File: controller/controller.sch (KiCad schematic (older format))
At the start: 46 parts, among them J1 Conn_01x25_Membrane, J2 Conn_01x04, SW1 SW_Push, SW2 SW_Push, U1 AMS1117-3.3, U2 STM32F303RCT6, U3 TPS2553DBVR, U4 USBLC6-2SC6, Y1 16MHz

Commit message: added solenoid driver
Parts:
- added J3: Conn_Solenoid_Driver, Connector_JST:JST_PH_S4B-PH-K_1x04_P2.00mm_Horizontal, symbol Connector_Generic:Conn_01x04
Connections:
- net labels added: SOLENOID_ENABLE, SOLENOID_TRIGGER
- wire segments 115 -> 117
- no-connect marks 19 -> 17
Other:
- note added: "GPIO PC13..PC15 output mode\ncurrent is limited"
- note removed: "Do not use GPIO PC13..PC15 in output mode\n(current is limited)"
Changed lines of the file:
@@
 	7925 5025 7450 5025
-$Comp
-L MCU_ST_STM32F3:STM32F303RCTx U2
-U 1 1 5FCE2F71
-P 4450 4325
-F 0 "U2" H 3875 2550 50  0000 C CNN
-F 1 "STM32F303RCT6" H 5025 2550 50  0000 C CNN
-F 2 "Package_QFP:LQFP-64_10x10mm_P0.5mm" H 3850 2625 50  0001 R CNN
-F 3 "https://datasheet.lcsc.com/szlcsc/1811182038_STMicroelectronics-STM32F303RCT6_C65361.pdf" H 4450 4325 50  0001 C CNN
-F 4 "C65361" H 4450 4325 50  0001 C CNN "LCSC"
-	1    4450 4325
-	1    0    0    -1
-$EndComp
 $Comp
 L Regulator_Linear:AMS1117-3.3 U1
@@
 NoConn ~ 5150 4225
 NoConn ~ 5150 4025
-Text Notes 5225 4175 0    50   ~ 0
-Do not use GPIO PC13..PC15 in output mode\n(current is limited)
+Text Notes 2625 6150 0    50   ~ 0
+GPIO PC13..PC15 output mode\ncurrent is limited
 Text GLabel 5350 3825 2    50   BiDi ~ 0
 USB_DM
@@
 NoConn ~ 3750 4225
 NoConn ~ 3750 4025
-NoConn ~ 3750 5725
 NoConn ~ 3750 5825
 NoConn ~ 3750 5925
@@
 NoConn ~ 5150 4725
 NoConn ~ 5150 4825
-NoConn ~ 5150 4925
 NoConn ~ 5150 5025
 NoConn ~ 5150 5125
@@
 	1    0    0    -1
 $EndComp
+$Comp
+L Connector_Generic:Conn_01x04 J3
+U 1 1 600024AB
+P 6100 7025
+F 0 "J3" H 6180 7017 50  0000 L CNN
+F 1 "Conn_Solenoid_Driver" H 6180 6926 50  0000 L CNN
+F 2 "Connector_JST:JST_PH_S4B-PH-K_1x04_P2.00mm_Horizontal" H 6100 7025 50  0001 C CNN
+F 3 "~" H 6100 7025 50  0001 C CNN
+F 4 "https://www.tme.eu/ro/katalog/conectori-de-semnal_30/?s_field=1000011&s_order=desc&search=jst&visible_params=412%2C2%2C6%2C613%2C422%2C7%2C426%2C9%2C416%2C77%2C18%2C32%2C1247%2C2555%2C418%2C419%2C1322%2C516%2C5%2C82%2C743%2C424%2C425%2C11%2C45&mapped_params=412%3A1443412%3B426%3A1443403%3B" H 6100 7025 50  0001 C CNN "Notes"
+	1    6100 7025
+	1    0    0    -1
+$EndComp
+$Comp
+L power:VBUS #PWR0108
+U 1 1 6000A0FD
+P 5825 6900
+F 0 "#PWR0108" H 5825 6750 50  0001 C CNN
+F 1 "VBUS" H 5950 7025 50  0000 C CNN
+F 2 "" H 5825 6900 50  0001 C CNN
+F 3 "" H 5825 6900 50  0001 C CNN
+	1    5825 6900
+	1    0    0    -1
+$EndComp
+Wire Wire Line
+	5825 6900 5825 6925
+Wire Wire Line
+	5825 6925 5900 6925
+$Comp
+L power:GND #PWR0109
+U 1 1 6000F2BB
+P 5900 7225
+F 0 "#PWR0109" H 5900 6975 50  0001 C CNN
+F 1 "GND" V 5905 7097 50  0000 R CNN
+F 2 "" H 5900 7225 50  0001 C CNN
+F 3 "" H 5900 7225 50  0001 C CNN
+	1    5900 7225
+	0    1    1    0
+$EndComp
+Text GLabel 5900 7125 0    50   BiDi ~ 0
+SOLENOID_ENABLE
+Text GLabel 5900 7025 0    50   BiDi ~ 0
+SOLENOID_TRIGGER
+Text GLabel 3750 5725 0    50   BiDi ~ 0
+SOLENOID_ENABLE
+Text GLabel 5150 4925 2    50   BiDi ~ 0
+SOLENOID_TRIGGER
+$Comp
+L MCU_ST_STM32F3:STM32F303RCTx U2
+U 1 1 5FCE2F71
+P 4450 4325
+F 0 "U2" H 3875 2550 50  0000 C CNN
+F 1 "STM32F303RCT6" H 5025 2550 50  0000 C CNN
+F 2 "Package_QFP:LQFP-64_10x10mm_P0.5mm" H 3850 2625 50  0001 R CNN
+F 3 "https://datasheet.lcsc.com/szlcsc/1811182038_STMicroelectronics-STM32F303RCT6_C65361.pdf" H 4450 4325 50  0001 C CNN
+F 4 "C65361" H 4450 4325 50  0001 C CNN "LCSC"
+	1    4450 4325
+	1    0    0    -1
+$EndComp

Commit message: added gpio header and other updates
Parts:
- added J4: Conn_01x04, Connector_PinHeader_2.54mm:PinHeader_1x04_P2.54mm_Vertical, symbol Connector_Generic:Conn_01x04
- added J5: Conn_01x07, Connector_PinHeader_2.54mm:PinHeader_1x07_P2.54mm_Vertical, symbol Connector_Generic:Conn_01x07
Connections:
- net labels added: GPIO_PA0, GPIO_PA1, GPIO_PA2, GPIO_PC3, UART_RX, UART_TX
- wire segments 117 -> 130
- no-connect marks 17 -> 12
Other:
- note added: "PA10 (UART RX) pulled high to make sure it's not\nmisinterpreted during bootloader mode."
- note added: "PA9 (UART TX) could be output during bootloader mode"
- note removed: "PA10 pulled high to make sure it's not\nmisinterpreted during bootloader mode."
- note removed: "PA9 could be output during bootloader mode"
- moved on the sheet: R8
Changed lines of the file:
@@
 Text GLabel 5150 3025 2    50   BiDi ~ 0
 MEMBRANE21
-Text GLabel 3750 4725 0    50   BiDi ~ 0
+Text GLabel 3550 4200 0    50   BiDi ~ 0
 MEMBRANE22
-Text GLabel 5150 2925 2    50   BiDi ~ 0
+Text GLabel 3750 4425 0    50   BiDi ~ 0
 MEMBRANE23
-Text GLabel 5150 2825 2    50   BiDi ~ 0
+Text GLabel 3750 4525 0    50   BiDi ~ 0
 MEMBRANE24
-Text GLabel 5150 2725 2    50   BiDi ~ 0
+Text GLabel 3750 4625 0    50   BiDi ~ 0
 MEMBRANE25
-NoConn ~ 5150 3625
-Text Notes 5225 3650 0    50   ~ 0
-PA9 could be output during bootloader mode
+Text Notes 5975 3650 0    50   ~ 0
+PA9 (UART TX) could be output during bootloader mode
 $Comp
 L Device:R R8
 U 1 1 6012C331
-P 5300 3725
-F 0 "R8" V 5250 3875 50  0000 C CNN
-F 1 "62k" V 5300 3725 50  0000 C CNN
-F 2 "Resistor_SMD:R_0805_2012Metric_Pad1.15x1.40mm_HandSolder" V 5230 3725 50  0001 C CNN
-F 3 "~" H 5300 3725 50  0001 C CNN
-F 4 "C17783" H 5300 3725 50  0001 C CNN "LCSC"
-	1    5300 3725
+P 6500 4000
+F 0 "R8" V 6450 4150 50  0000 C CNN
+F 1 "62k" V 6500 4000 50  0000 C CNN
+F 2 "Resistor_SMD:R_0805_2012Metric_Pad1.15x1.40mm_HandSolder" V 6430 4000 50  0001 C CNN
+F 3 "~" H 6500 4000 50  0001 C CNN
+F 4 "C17783" H 6500 4000 50  0001 C CNN "LCSC"
+	1    6500 4000
 	0    1    1    0
 $EndComp
@@
 L power:+3.3V #PWR0105
 U 1 1 60130C5B
-P 5450 3725
-F 0 "#PWR0105" H 5450 3575 50  0001 C CNN
-F 1 "+3.3V" V 5465 3853 50  0000 L CNN
-F 2 "" H 5450 3725 50  0001 C CNN
-F 3 "" H 5450 3725 50  0001 C CNN
-	1    5450 3725
+P 6650 4000
+F 0 "#PWR0105" H 6650 3850 50  0001 C CNN
+F 1 "+3.3V" V 6665 4128 50  0000 L CNN
+F 2 "" H 6650 4000 50  0001 C CNN
+F 3 "" H 6650 4000 50  0001 C CNN
+	1    6650 4000
 	0    1    1    0
 $EndComp
-Text Notes 5850 3825 0    50   ~ 0
-PA10 pulled high to make sure it's not\nmisinterpreted during bootloader mode.
+Text Notes 6075 3825 0    50   ~ 0
+PA10 (UART RX) pulled high to make sure it's not\nmisinterpreted during bootloader mode.
 Text GLabel 6750 5025 0    50   BiDi ~ 0
 LEDDRV1
@@
 LEDDRV3
 NoConn ~ 3750 4225
-NoConn ~ 3750 4025
 NoConn ~ 3750 5825
 NoConn ~ 3750 5925
@@
 Wire Wire Line
 	7975 6100 8025 6100
-NoConn ~ 3750 4425
-NoConn ~ 3750 4525
-NoConn ~ 3750 4625
 NoConn ~ 5150 4725
 NoConn ~ 5150 4825
@@
 	1    0    0    -1
 $EndComp
+Wire Wire Line
+	3550 4200 3600 4200
+Wire Wire Line
+	3600 4200 3600 4025
+Wire Wire Line
+	3600 4025 3750 4025
+$Comp
+L Connector_Generic:Conn_01x04 J4
+U 1 1 5FDF4DBB
+P 7200 4550
+F 0 "J4" H 7118 4125 50  0000 C CNN
+F 1 "Conn_01x04" H 7118 4216 50  0000 C CNN
+F 2 "Connector_PinHeader_2.54mm:PinHeader_1x04_P2.54mm_Vertical" H 7200 4550 50  0001 C CNN
+F 3 "~" H 7200 4550 50  0001 C CNN
+	1    7200 4550
+	-1   0    0    1
+$EndComp
+Text GLabel 5150 3625 2    50   BiDi ~ 0
+UART_TX
+Text GLabel 7400 4550 2    50   BiDi ~ 0
+UART_TX
+Text GLabel 5150 3725 2    50   BiDi ~ 0
+UART_RX
+Text GLabel 6350 4000 0    50   BiDi ~ 0
+UART_RX
+Text GLabel 7400 4450 2    50   BiDi ~ 0
+UART_RX
+$Comp
+L power:GND #PWR030
+U 1 1 5FE1A17C
+P 7675 4700
+F 0 "#PWR030" H 7675 4450 50  0001 C CNN
+F 1 "GND" H 7675 4550 50  0000 C CNN
+F 2 "" H 7675 4700 50  0001 C CNN
+F 3 "" H 7675 4700 50  0001 C CNN
+	1    7675 4700
+	1    0    0    -1
+$EndComp
+$Comp
+L power:+3.3V #PWR029
+U 1 1 5FE1A75A
+P 7675 4325
+F 0 "#PWR029" H 7675 4175 50  0001 C CNN
+F 1 "+3.3V" H 7690 4498 50  0000 C CNN
+F 2 "" H 7675 4325 50  0001 C CNN
+F 3 "" H 7675 4325 50  0001 C CNN
+	1    7675 4325
+	1    0    0    -1
+$EndComp
+Wire Wire Line
+	7675 4350 7675 4325
+Text GLabel 5150 2725 2    50   BiDi ~ 0
+GPIO_PA0
+Text GLabel 5150 2825 2    50   BiDi ~ 0
+GPIO_PA1
+Text GLabel 5150 2925 2    50   BiDi ~ 0
+GPIO_PA2
+Text GLabel 3750 4725 0    50   BiDi ~ 0
+GPIO_PC3
+Text GLabel 10275 5450 0    50   BiDi ~ 0
+GPIO_PA0
+Text GLabel 10275 5550 0    50   BiDi ~ 0
+GPIO_PA1
+Text GLabel 10275 5750 0    50   BiDi ~ 0
+GPIO_PA2
+Text GLabel 10275 5850 0    50   BiDi ~ 0
+GPIO_PC3
+$Comp
+L power:GND #PWR032
+U 1 1 5FE70830
+P 9750 5725
+F 0 "#PWR032" H 9750 5475 50  0001 C CNN
+F 1 "GND" H 9750 5575 50  0000 C CNN
+F 2 "" H 9750 5725 50  0001 C CNN
+F 3 "" H 9750 5725 50  0001 C CNN
+	1    9750 5725
+	1    0    0    -1
+$EndComp
+$Comp
+L power:+3.3V #PWR031
+U 1 1 5FE7203C
+P 9500 5850
+F 0 "#PWR031" H 9500 5700 50  0001 C CNN
+F 1 "+3.3V" H 9515 6023 50  0000 C CNN
+F 2 "" H 9500 5850 50  0001 C CNN
+F 3 "" H 9500 5850 50  0001 C CNN
+	1    9500 5850
+	1    0    0    -1
+$EndComp
+$Comp
+L Connector_Generic:Conn_01x07 J5
+U 1 1 5FEB4462
+P 10475 5650
+F 0 "J5" H 10555 5692 50  0000 L CNN
+F 1 "Conn_01x07" H 10555 5601 50  0000 L CNN
+F 2 "Connector_PinHeader_2.54mm:PinHeader_1x07_P2.54mm_Vertical" H 10475 5650 50  0001 C CNN
+F 3 "~" H 10475 5650 50  0001 C CNN
+	1    10475 5650
+	1    0    0    -1
+$EndComp
+$Comp
+L power:VBUS #PWR033
+U 1 1 5FEC2379
+P 10175 5275
+F 0 "#PWR033" H 10175 5125 50  0001 C CNN
+F 1 "VBUS" H 10190 5448 50  0000 C CNN
+F 2 "" H 10175 5275 50  0001 C CNN
+F 3 "" H 10175 5275 50  0001 C CNN
+	1    10175 5275
+	1    0    0    -1
+$EndComp
+Wire Wire Line
+	10175 5275 10175 5350
+Wire Wire Line
+	10175 5350 10275 5350
+Wire Wire Line
+	9750 5725 9750 5650
+Wire Wire Line
+	9750 5650 10275 5650
+Wire Wire Line
+	9500 5950 9500 5850
+Wire Wire Line
+	9500 5950 10275 5950
+Wire Wire Line
+	7400 4350 7675 4350
+Wire Wire Line
+	7400 4650 7675 4650
+Wire Wire Line
+	7675 4650 7675 4700
 $EndSCHEMATC

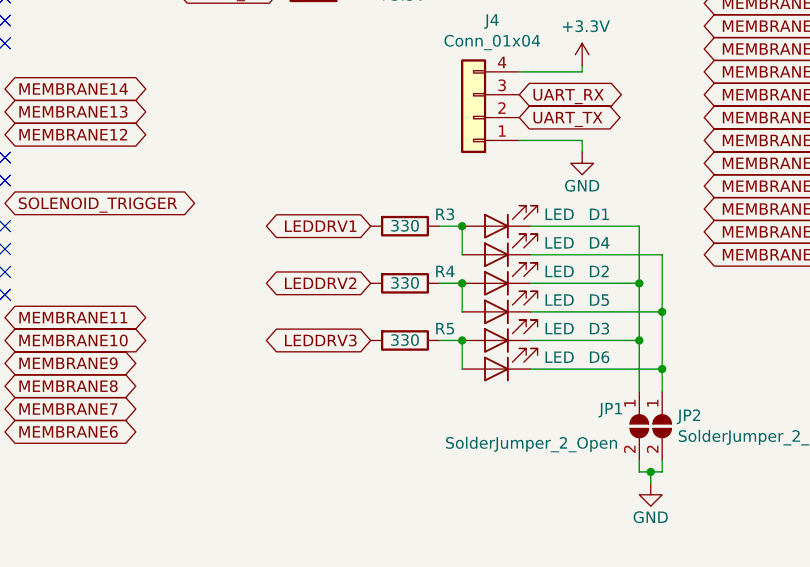
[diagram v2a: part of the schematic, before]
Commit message: LED current limit resistors changed to 47 ohm
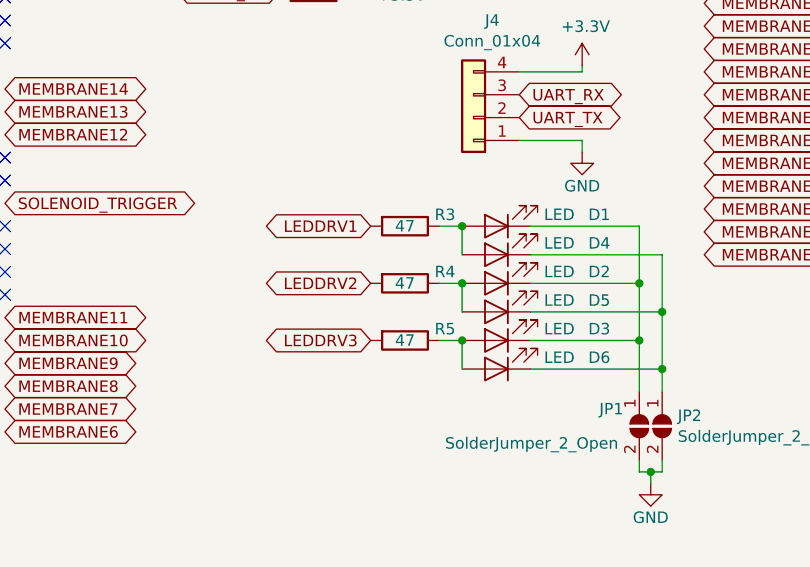
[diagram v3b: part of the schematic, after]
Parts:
- R3, R4, R5: value 330 -> 47; LCSC C17630 -> C17714
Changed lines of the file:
@@
 P 6900 5025
 F 0 "R3" V 6850 5200 50  0000 C CNN
-F 1 "330" V 6900 5025 50  0000 C CNN
+F 1 "47" V 6900 5025 50  0000 C CNN
 F 2 "Resistor_SMD:R_0805_2012Metric_Pad1.15x1.40mm_HandSolder" V 6830 5025 50  0001 C CNN
 F 3 "~" H 6900 5025 50  0001 C CNN
-F 4 "C17630" H 6900 5025 50  0001 C CNN "LCSC"
+F 4 "C17714" H 6900 5025 50  0001 C CNN "LCSC"
 	1    6900 5025
 	0    1    1    0
@@
 P 6900 5275
 F 0 "R4" V 6850 5450 50  0000 C CNN
-F 1 "330" V 6900 5275 50  0000 C CNN
+F 1 "47" V 6900 5275 50  0000 C CNN
 F 2 "Resistor_SMD:R_0805_2012Metric_Pad1.15x1.40mm_HandSolder" V 6830 5275 50  0001 C CNN
 F 3 "~" H 6900 5275 50  0001 C CNN
-F 4 "C17630" H 6900 5275 50  0001 C CNN "LCSC"
+F 4 "C17714" H 6900 5275 50  0001 C CNN "LCSC"
 	1    6900 5275
 	0    1    1    0
@@
 P 6900 5525
 F 0 "R5" V 6850 5700 50  0000 C CNN
-F 1 "330" V 6900 5525 50  0000 C CNN
+F 1 "47" V 6900 5525 50  0000 C CNN
 F 2 "Resistor_SMD:R_0805_2012Metric_Pad1.15x1.40mm_HandSolder" V 6830 5525 50  0001 C CNN
 F 3 "~" H 6900 5525 50  0001 C CNN
-F 4 "C17630" H 6900 5525 50  0001 C CNN "LCSC"
+F 4 "C17714" H 6900 5525 50  0001 C CNN "LCSC"
 	1    6900 5525
 	0    1    1    0
@@
 F 1 "LED" H 7025 4975 50  0000 C CNN
 F 2 "LED_SMD:LED_0805_2012Metric_Pad1.15x1.40mm_HandSolder" H 7300 5025 50  0001 C CNN
-F 3 "~" H 7300 5025 50  0001 C CNN
+F 3 "https://datasheet.lcsc.com/szlcsc/Hubei-KENTO-Elec-17-21SUYC-TR8_C2296.pdf" H 7300 5025 50  0001 C CNN
 F 4 "C2296" H 7300 5025 50  0001 C CNN "LCSC"
 	1    7300 5025
@@
 F 1 "LED" H 7025 5225 50  0000 C CNN
 F 2 "LED_SMD:LED_0805_2012Metric_Pad1.15x1.40mm_HandSolder" H 7300 5275 50  0001 C CNN
-F 3 "~" H 7300 5275 50  0001 C CNN
+F 3 "https://datasheet.lcsc.com/szlcsc/Hubei-KENTO-Elec-17-21SUYC-TR8_C2296.pdf" H 7300 5275 50  0001 C CNN
 F 4 "C2296" H 7300 5275 50  0001 C CNN "LCSC"
 	1    7300 5275
@@
 F 1 "LED" H 7025 5475 50  0000 C CNN
 F 2 "LED_SMD:LED_0805_2012Metric_Pad1.15x1.40mm_HandSolder" H 7300 5525 50  0001 C CNN
-F 3 "~" H 7300 5525 50  0001 C CNN
+F 3 "https://datasheet.lcsc.com/szlcsc/Hubei-KENTO-Elec-17-21SUYC-TR8_C2296.pdf" H 7300 5525 50  0001 C CNN
 F 4 "C2296" H 7300 5525 50  0001 C CNN "LCSC"
 	1    7300 5525
@@
 F 1 "LED" H 7025 5100 50  0000 C CNN
 F 2 "LED_SMD:LED_0805_2012Metric_Pad1.15x1.40mm_HandSolder" H 7300 5150 50  0001 C CNN
-F 3 "~" H 7300 5150 50  0001 C CNN
+F 3 "https://datasheet.lcsc.com/szlcsc/Hubei-KENTO-Elec-17-21SUYC-TR8_C2296.pdf" H 7300 5150 50  0001 C CNN
 F 4 "C2296" H 7300 5150 50  0001 C CNN "LCSC"
 	1    7300 5150
@@
 F 1 "LED" H 7025 5350 50  0000 C CNN
 F 2 "LED_SMD:LED_0805_2012Metric_Pad1.15x1.40mm_HandSolder" H 7300 5400 50  0001 C CNN
-F 3 "~" H 7300 5400 50  0001 C CNN
+F 3 "https://datasheet.lcsc.com/szlcsc/Hubei-KENTO-Elec-17-21SUYC-TR8_C2296.pdf" H 7300 5400 50  0001 C CNN
 F 4 "C2296" H 7300 5400 50  0001 C CNN "LCSC"
 	1    7300 5400
@@
 F 1 "LED" H 7025 5600 50  0000 C CNN
 F 2 "LED_SMD:LED_0805_2012Metric_Pad1.15x1.40mm_HandSolder" H 7300 5650 50  0001 C CNN
-F 3 "~" H 7300 5650 50  0001 C CNN
+F 3 "https://datasheet.lcsc.com/szlcsc/Hubei-KENTO-Elec-17-21SUYC-TR8_C2296.pdf" H 7300 5650 50  0001 C CNN
 F 4 "C2296" H 7300 5650 50  0001 C CNN "LCSC"
 	1    7300 5650

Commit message: more updates
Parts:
- added J6: Conn_01x06, Connector_PinHeader_1.27mm:PinHeader_1x06_P1.27mm_Vertical, symbol Connector_Generic:Conn_01x06
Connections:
- net labels added: GPIO_PA14, GPIO_PA15, GPIO_PB3, GPIO_PB4, GPIO_PD2
- wire segments 130 -> 135
- no-connect marks 12 -> 7
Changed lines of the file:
@@
 Wire Wire Line
 	9225 1225 10050 1225
-NoConn ~ 5150 4125
-NoConn ~ 5150 4225
 NoConn ~ 5150 4025
 Text Notes 2625 6150 0    50   ~ 0
@@
 Text GLabel 3750 5425 0    50   BiDi ~ 0
 LEDDRV3
-NoConn ~ 3750 4225
 NoConn ~ 3750 5825
 NoConn ~ 3750 5925
@@
 Wire Wire Line
 	7975 6100 8025 6100
-NoConn ~ 5150 4725
-NoConn ~ 5150 4825
 NoConn ~ 5150 5025
 NoConn ~ 5150 5125
@@
 Wire Wire Line
 	7675 4650 7675 4700
+Text GLabel 10400 4275 0    50   BiDi ~ 0
+GPIO_PA15
+Text GLabel 10400 4375 0    50   BiDi ~ 0
+GPIO_PA14
+Text GLabel 10400 4475 0    50   BiDi ~ 0
+GPIO_PD2
+Text GLabel 10400 4675 0    50   BiDi ~ 0
+GPIO_PB3
+Text GLabel 10400 4775 0    50   BiDi ~ 0
+GPIO_PB4
+Text GLabel 5150 4225 2    50   BiDi ~ 0
+GPIO_PA15
+Text GLabel 5150 4125 2    50   BiDi ~ 0
+GPIO_PA14
+Text GLabel 3550 4300 0    50   BiDi ~ 0
+GPIO_PD2
+Text GLabel 5150 4725 2    50   BiDi ~ 0
+GPIO_PB3
+Text GLabel 5150 4825 2    50   BiDi ~ 0
+GPIO_PB4
+Wire Wire Line
+	3550 4300 3675 4300
+Wire Wire Line
+	3675 4300 3675 4225
+Wire Wire Line
+	3675 4225 3750 4225
+$Comp
+L Connector_Generic:Conn_01x06 J6
+U 1 1 5FE2D298
+P 10600 4475
+F 0 "J6" H 10680 4467 50  0000 L CNN
+F 1 "Conn_01x06" H 10680 4376 50  0000 L CNN
+F 2 "Connector_PinHeader_1.27mm:PinHeader_1x06_P1.27mm_Vertical" H 10600 4475 50  0001 C CNN
+F 3 "~" H 10600 4475 50  0001 C CNN
+	1    10600 4475
+	1    0    0    -1
+$EndComp
+$Comp
+L power:GND #PWR?
+U 1 1 5FE37C14
+P 9850 4625
+F 0 "#PWR?" H 9850 4375 50  0001 C CNN
+F 1 "GND" H 9850 4475 50  0000 C CNN
+F 2 "" H 9850 4625 50  0001 C CNN
+F 3 "" H 9850 4625 50  0001 C CNN
+	1    9850 4625
+	1    0    0    -1
+$EndComp
+Wire Wire Line
+	9850 4625 9850 4575
+Wire Wire Line
+	9850 4575 10400 4575
 $EndSCHEMATC

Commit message: Added version 1.0b, and exported 3mm version gerber
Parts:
- removed J4: Conn_01x04, Connector_PinHeader_2.54mm:PinHeader_1x04_P2.54mm_Vertical, symbol Connector_Generic:Conn_01x04
- removed U2: STM32F303RCT6, Package_QFP:LQFP-64_10x10mm_P0.5mm, symbol MCU_ST_STM32F3:STM32F303RCTx
- added C18: 4.7uF, Capacitor_SMD:C_0805_2012Metric_Pad1.15x1.40mm_HandSolder, symbol Device:C
- added R10, R11, R12, R9: 62k, Resistor_SMD:R_0805_2012Metric_Pad1.15x1.40mm_HandSolder, symbol Device:R
- added U2: STM32F446RETx, Package_QFP:LQFP-64_10x10mm_P0.5mm, symbol MCU_ST_STM32F4:STM32F446RETx
- R6: value 1.5k -> 62k; LCSC C4310 -> C17783
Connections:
- net labels added: BOOT0, LEDDRV2_USART3RX_BL, MEMBRANE19_PA5, MEMBRANE1_PA10, MEMBRANE4_PC9, MEMBRANE6_PC7, NRST, OSCI, OSCO, OSCO_RES, SOLENOID_TRIGGER_CAN_RX_BL
- net labels removed: GPIO_PC3, LEDDRV2, MEMBRANE1, MEMBRANE19, MEMBRANE4, MEMBRANE6, SOLENOID_TRIGGER, UART_RX, UART_TX
- wire segments 135 -> 130
- no-connect marks 7 -> 5
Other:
- note added: "BOOT1"
- note added: "Notes on various special GPIOs of this chip:\n\n* The following can be output during bootloader mode,\n make sure nothing is driving into them during programming:\n * PA9 (USART1 TX), PB10 (maybe USART3 TX), PC10\n (USART3 TX), PB13 (CAN2_TX), PB14 (SPI2_MISO), PA6 (SPI1_MISO)\n\n* The following pins need to be stable and unchanging during\n programming in order to guarantee that DFU mode activat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"
- note removed: "Bootloader document says,\nclock must be one of:\n24,18,16,12,9,8,6,4,3 MHz\n"
- note removed: "GPIO PC13..PC15 output mode\ncurrent is limited"
- note removed: "PA10 (UART RX) pulled high to make sure it's not\nmisinterpreted during bootloader mode."
- note removed: "PA9 (UART TX) could be output during bootloader mode"
- moved on the sheet: J1, J2, J3, R2, R8

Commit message: Added v1.1b version
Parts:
- removed J5: Conn_01x07, Connector_PinHeader_2.54mm:PinHeader_1x07_P2.54mm_Vertical, symbol Connector_Generic:Conn_01x07
- removed JP1: SolderJumper_2_Open, controller:shortable, symbol Jumper:SolderJumper_2_Open
- removed SW1, SW2: SW_Push, controller:TS342A2PWZ, symbol Switch:SW_Push
- added C19: 100nF, Capacitor_SMD:C_0805_2012Metric_Pad1.15x1.40mm_HandSolder, symbol Device:C
- added C20: 1uF, Capacitor_SMD:C_0805_2012Metric_Pad1.15x1.40mm_HandSolder, symbol Device:C
- added J4: Conn_01x01, controller:PinHeader_1x01_P1.27mm_Vertical_mod_no_courtyard_no_ref, symbol Connector_Generic:Conn_01x01
- added JP1: SolderJumper_2_Bridged, controller:shortable_shorted, symbol Jumper:SolderJumper_2_Bridged
- added Q1: Q_PMOS_GSD AO3401A, Package_TO_SOT_SMD:SOT-23, symbol Device:Q_PMOS_GSD
- added Q2, Q3: Q_NMOS_GSD 2N7002, Package_TO_SOT_SMD:SOT-23, symbol Device:Q_NMOS_GSD
- added R13, R14, R15, R17, R18: 2k, Resistor_SMD:R_0805_2012Metric_Pad1.15x1.40mm_HandSolder, symbol Device:R
- added R16: 390, Resistor_SMD:R_0805_2012Metric_Pad1.15x1.40mm_HandSolder, symbol Device:R
- added SW1: SW_Push, controller:switch_K2-1187SQ-A4SW-06, symbol 4pinpushbutton:SW_Push
- added U5: 24LC64, Package_SO:SOIC-8_3.9x4.9mm_P1.27mm, symbol Memory_EEPROM:24LC64
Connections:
- net labels added: BOOT0_DRV, BottomLightsGround, LD1R, LD2R, LD3R, TopLightsGround, VCAP_1
- wire segments 130 -> 147
- no-connect marks 5 -> 7
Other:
- note removed: "TODO BULK CAPS, maybe fuse\n"
- moved on the sheet: C10, C5, C6, C7, J6

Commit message: Prepare the design for release
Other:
- note added: "Copyright Andrei Purdea 2021.\nThis source describes Open Hardware and is licensed under the CERN-OHL-P v2\nYou may redistribute and modify this documentation and make products using it under the terms of the\nCERN-OHL-P v2 (https:/cern.ch/cern-ohl).\nThis documentation is distributed WITHOUT ANY EXPRESS OR IMPLIED WARRANTY, INCLUDING OF\nMERCHANTABILITY, SATISFACTORY QUALITY AND FITNESS FOR A PA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"
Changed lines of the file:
@@
 encoding utf-8
 Sheet 1 1
-Title ""
+Title "OverNumpad Controller"
 Date ""
 Rev ""
@@
 NoConn ~ 1450 3725
 NoConn ~ 1650 4225
+Text Notes 7025 7075 0    43   ~ 0
+Copyright Andrei Purdea 2021.\nThis source describes Open Hardware and is licensed under the CERN-OHL-P v2\nYou may redistribute and modify this documentation and make products using it under the terms of the\nCERN-OHL-P v2 (https:/cern.ch/cern-ohl).\nThis documentation is distributed WITHOUT ANY EXPRESS OR IMPLIED WARRANTY, INCLUDING OF\nMERCHANTABILITY, SATISFACTORY QUALITY AND FITNESS FOR A PARTICULAR PURPOSE. Please see the\nCERN-OHL-P v2 for applicable conditions
 $EndSCHEMATC

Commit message: Replacing LCSC reference for P-channel mosfet, to same transistor from different manufacturer.
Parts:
- Q1: LCSC C15127 -> C700954
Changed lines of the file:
@@
 F 2 "Package_TO_SOT_SMD:SOT-23" H 2225 2700 50  0001 C CNN
 F 3 "~" H 2025 2600 50  0001 C CNN
-F 4 "C15127" H 2025 2600 50  0001 C CNN "LCSC"
+F 4 "C700954" H 2025 2600 50  0001 C CNN "LCSC"
 	1    2025 2600
 	1    0    0    1
